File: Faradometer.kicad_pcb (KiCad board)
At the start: 2 copper layers, 26 x 22.2 mm, 20 parts, among them J101 Conn_01x02_Pin, J102 Conn_01x03_Pin, U101 TL072CP, U102 TL072CP

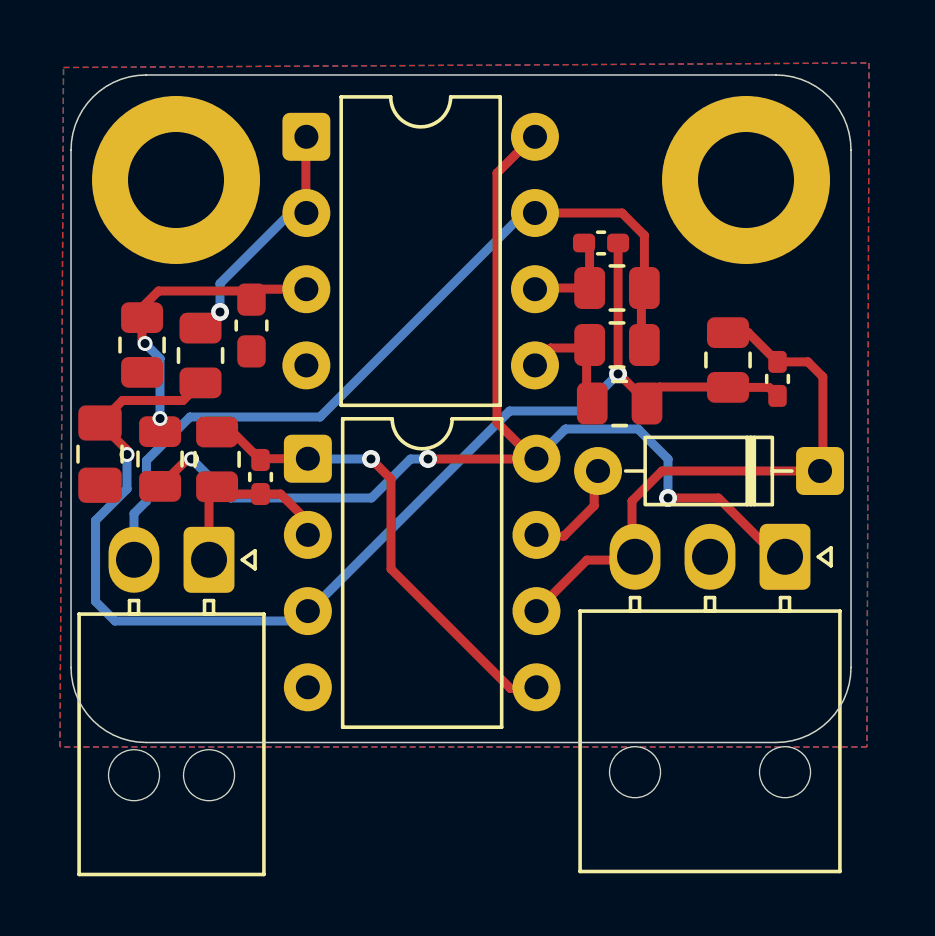
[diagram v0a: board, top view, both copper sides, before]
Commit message: Add .gitignore for KiCad junk files
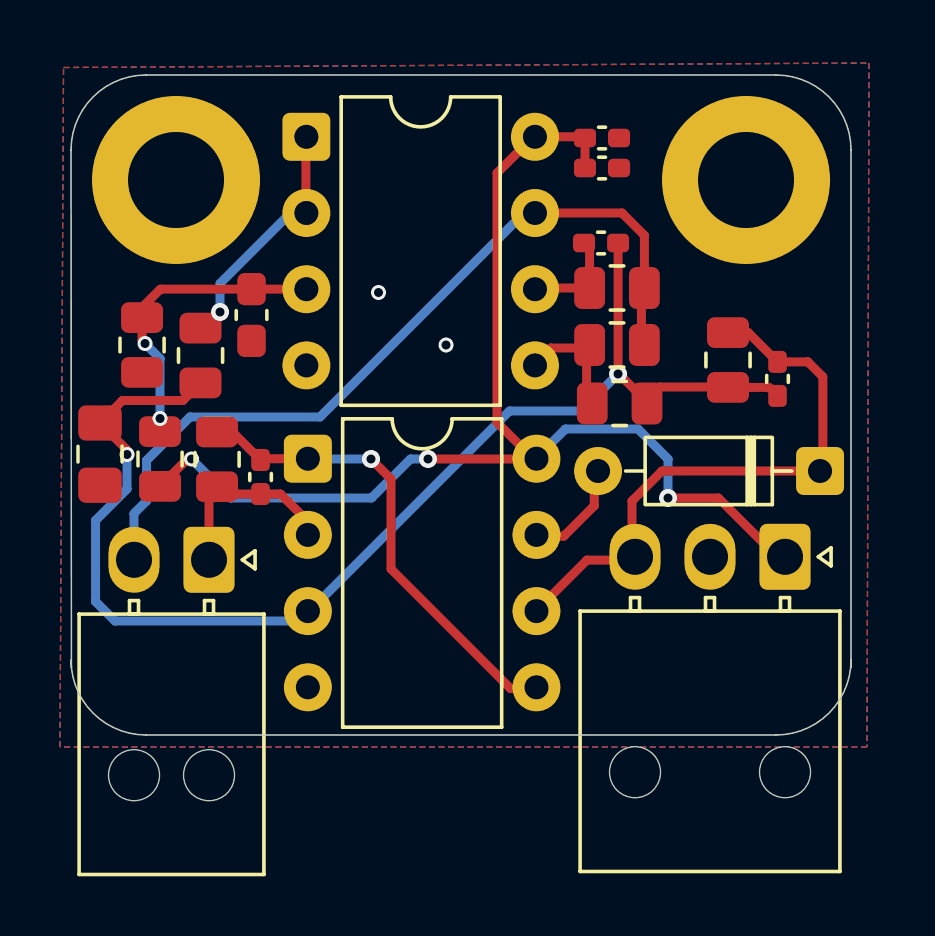
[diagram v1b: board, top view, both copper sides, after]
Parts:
- added C1: 100nF, Capacitor_SMD:C_0402_1005Metric_Pad0.74x0.62mm_HandSolder, F.Cu at (141.7, 65.1)
- added C2: 100nF, Capacitor_SMD:C_0402_1005Metric_Pad0.74x0.62mm_HandSolder, F.Cu at (141.7, 66.1)
- moved C101 0.35 mm to (130.0, 71.0)
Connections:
- net /U2 1 out renamed Net-(U102C-+)
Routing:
- net +12V: track 37.0 -> 39.7 mm
- net GND: vias 0 -> 2
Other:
- board size 26 x 22.2 mm -> 26 x 22 mm

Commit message: decoupling capacitor connection
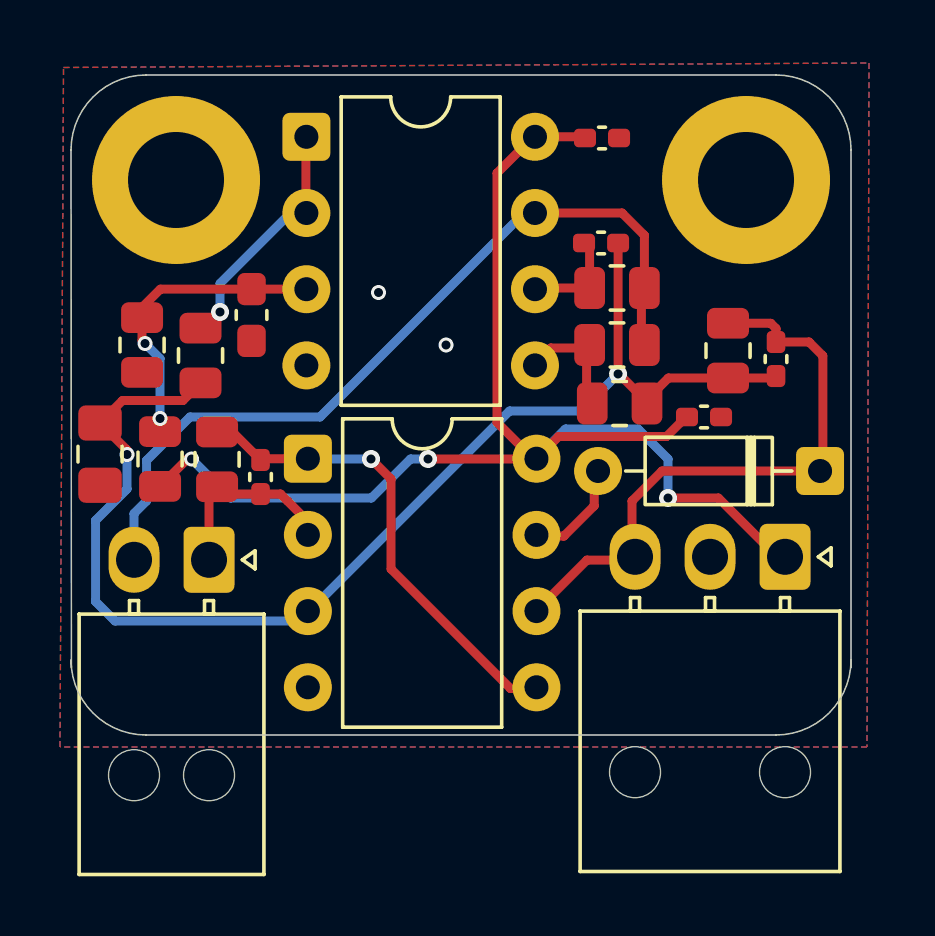
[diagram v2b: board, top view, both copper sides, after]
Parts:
- moved C2 8.97 mm to (145.1, 74.4)
- moved C105 0.66 mm to (147.5, 72.5)
- moved R108 0.31 mm to (145.9, 72.2)
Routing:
- net +12V: track 39.7 -> 44.3 mm
- net /V Out: track 19.6 -> 20.4 mm
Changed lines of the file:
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@@
 	(footprint "Capacitor_SMD:C_0402_1005Metric_Pad0.74x0.62mm_HandSolder"
 		(layer "F.Cu")
-		(at 147.55 73.13 -90)
+		(at 147.5 72.4675 -90)
 		(descr "Capacitor SMD 0402 (1005 Metric), square (rectangular) end terminal, IPC-7351 nominal with elongated pad for handsoldering. (Body size source: IPC-SM-782 page 76, https://www.pcb-3d.com/wordpress/wp-content/uploads/ipc-sm-782a_amendment_1_and_2.pdf), generated with kicad-footprint-generator")
 		(tags "capacitor handsolder")
@@
 	(footprint "Capacitor_SMD:C_0402_1005Metric_Pad0.74x0.62mm_HandSolder"
 		(layer "F.Cu")
-		(at 141.7 66.1)
+		(at 145.1 74.4)
 		(descr "Capacitor SMD 0402 (1005 Metric), square (rectangular) end terminal, IPC-7351 nominal with elongated pad for handsoldering. (Body size source: IPC-SM-782 page 76, https://www.pcb-3d.com/wordpress/wp-content/uploads/ipc-sm-782a_amendment_1_and_2.pdf), generated with kicad-footprint-generator")
 		(tags "capacitor handsolder")
@@
 			(at 0 1.16 0)
 			(layer "F.Fab")
+			(hide yes)
 			(effects
 				(font
@@
 	(footprint "Resistor_SMD:R_0805_2012Metric"
 		(layer "F.Cu")
-		(at 145.9 72.5 90)
+		(at 145.9 72.1875 90)
 		(descr "Resistor SMD 0805 (2012 Metric), square (rectangular) end terminal, IPC-7351 nominal, (Body size source: IPC-SM-782 page 72, https://www.pcb-3d.com/wordpress/wp-content/uploads/ipc-sm-782a_amendment_1_and_2.pdf), generated with kicad-footprint-generator")
 		(tags "resistor")
@@
 	)
 	(segment
-		(start 147.265 73.4125)
-		(end 147.55 73.6975)
+		(start 143.2 73.8125)
+		(end 143.9125 73.1)
 		(width 0.3)
 		(layer "F.Cu")
@@
 	)
 	(segment
-		(start 143.6125 73.4)
-		(end 145.8875 73.4)
+		(start 142.235 72.965)
+		(end 142.235 68.6)
 		(width 0.3)
 		(layer "F.Cu")
@@
 	)
 	(segment
-		(start 142.235 72.965)
-		(end 142.235 68.6)
+		(start 125.8675 75.5)
+		(end 125.8675 75.65)
 		(width 0.3)
 		(layer "F.Cu")
@@
 	)
 	(segment
-		(start 125.8675 75.5)
-		(end 125.8675 75.65)
+		(start 145.9 73.1)
+		(end 147.465 73.1)
 		(width 0.3)
 		(layer "F.Cu")
@@
 	)
 	(segment
-		(start 143.2 73.8125)
-		(end 143.6125 73.4)
-		(width 0.3)
-		(layer "F.Cu")
-		(net 1)
-	)
-	(segment
 		(start 125.7175 73.85)
 		(end 124.9675 74.6)
@@
 	)
 	(segment
-		(start 145.9 73.4125)
-		(end 147.265 73.4125)
+		(start 143.9125 73.1)
+		(end 145.9 73.1)
 		(width 0.3)
 		(layer "F.Cu")
@@
 	)
 	(segment
-		(start 145.8875 73.4)
-		(end 145.9 73.4125)
+		(start 147.465 73.1)
+		(end 147.5 73.135)
+		(width 0.3)
+		(layer "F.Cu")
+		(net 1)
+	)
+	(segment
+		(start 145.8875 73.0875)
+		(end 145.9 73.1)
 		(width 0.3)
 		(layer "F.Cu")
@@
 	)
 	(segment
-		(start 149.06 73.06)
-		(end 148.5625 72.5625)
+		(start 147.325 71.275)
+		(end 145.9 71.275)
 		(width 0.3)
 		(layer "F.Cu")
@@
 	)
 	(segment
-		(start 142.7 77.2)
-		(end 143.7 76.2)
+		(start 147.5 71.9)
+		(end 148.6 71.9)
 		(width 0.3)
 		(layer "F.Cu")
@@
 	)
 	(segment
-		(start 141.1975 79.17)
-		(end 142.65 79.17)
+		(start 139.4575 80.91)
+		(end 139.45 80.91)
 		(width 0.3)
 		(layer "F.Cu")
@@
 	)
 	(segment
-		(start 139.45 80.91)
+		(start 141.1975 79.17)
 		(end 139.4575 80.91)
 		(width 0.3)
@@
 	)
 	(segment
-		(start 148.5625 72.5625)
-		(end 147.55 72.5625)
+		(start 142.65 79.17)
+		(end 141.1975 79.17)
 		(width 0.3)
 		(layer "F.Cu")
@@
 	)
 	(segment
-		(start 142.65 79.17)
-		(end 142.7 79.12)
+		(start 147.5 71.45)
+		(end 147.325 71.275)
 		(width 0.3)
 		(layer "F.Cu")
@@
 	)
 	(segment
-		(start 139.4575 80.91)
-		(end 141.1975 79.17)
+		(start 143.7 76.2)
+		(end 142.7 77.2)
 		(width 0.3)
 		(layer "F.Cu")
@@
 	)
 	(segment
-		(start 142.7 79.12)
-		(end 142.7 77.2)
+		(start 147.5 71.9)
+		(end 147.5 71.45)
 		(width 0.3)
 		(layer "F.Cu")
@@
 	)
 	(segment
-		(start 143.7 76.2)
+		(start 149.06 72.36)
 		(end 149.06 76.2)
 		(width 0.3)
@@
 	)
 	(segment
-		(start 149.06 76.2)
-		(end 149.06 73.06)
+		(start 148.6 71.9)
+		(end 149.06 72.36)
+		(width 0.3)
+		(layer "F.Cu")
+		(net 5)
+	)
+	(segment
+		(start 142.7 79.12)
+		(end 142.65 79.17)
 		(width 0.3)
 		(layer "F.Cu")
@@
 	)
 	(segment
-		(start 145.9 71.5875)
-		(end 146.575 71.5875)
+		(start 142.7 77.2)
+		(end 142.7 79.12)
 		(width 0.3)
 		(layer "F.Cu")
@@
 	)
 	(segment
-		(start 146.575 71.5875)
-		(end 147.55 72.5625)
+		(start 149.06 76.2)
+		(end 143.7 76.2)
 		(width 0.3)
 		(layer "F.Cu")
@@
 	)
 	(segment
-		(start 141.1325 66.1)
-		(end 141.1325 65.1)
+		(start 140.255 75.05)
+		(end 139.515 75.79)
+		(width 0.3)
+		(layer "F.Cu")
+		(net 9)
+	)
+	(segment
+		(start 143.85 75.05)
+		(end 140.255 75.05)
 		(width 0.3)
 		(layer "F.Cu")
@@
 	)
 	(segment
+		(start 144.5325 74.4)
+		(end 144.5 74.4)
+		(width 0.3)
+		(layer "F.Cu")
+		(net 9)
+	)
+	(segment
 		(start 138.2 74.58)
 		(end 139.45 75.83)
@@
 		(width 0.3)
 		(layer "F.Cu")
+		(net 9)
+	)
+	(segment
+		(start 144.5 74.4)
+		(end 143.85 75.05)
+		(width 0.3)
+		(layer "F.Cu")

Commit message: capacitor rearrangements
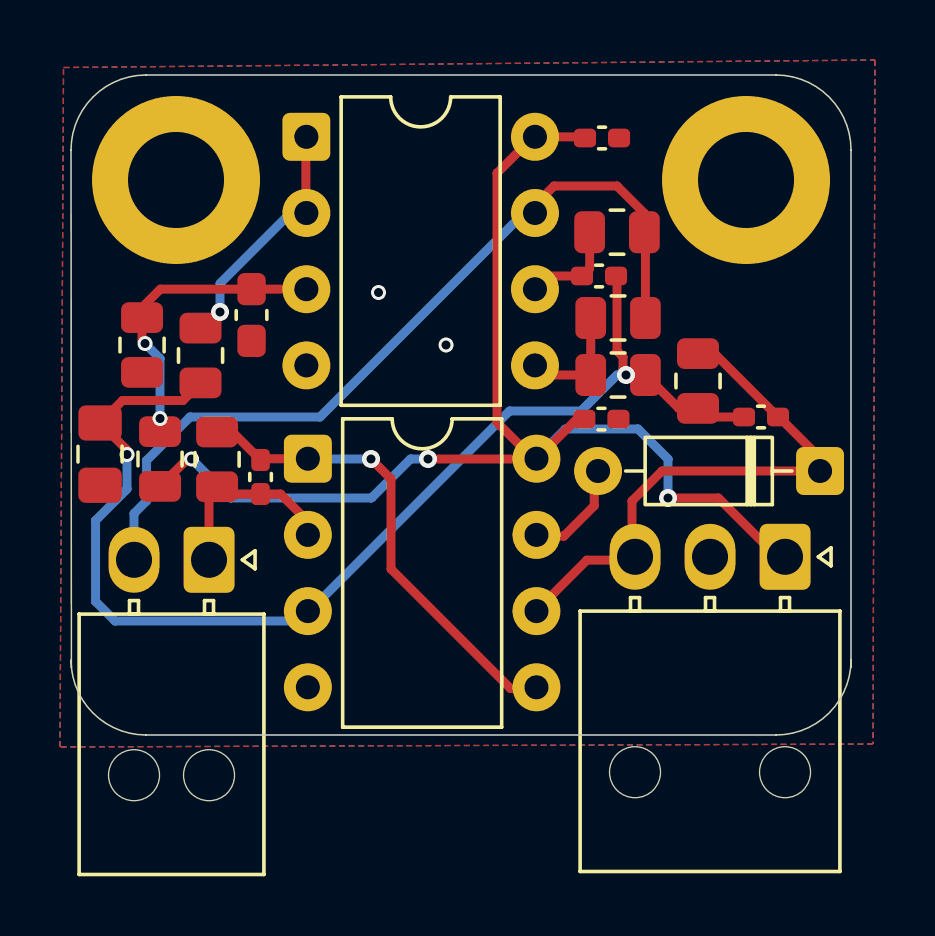
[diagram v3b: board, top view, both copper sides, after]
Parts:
- moved C2 3.42 mm to (141.7, 74.5)
- moved C105 2.00 mm to (147.0, 74.4), turned to 180 degrees
- moved R107 1.86 mm to (142.2, 68.2)
- moved R108 1.42 mm to (144.9, 73.2)
- moved C104 1.10 mm to (141.6, 69.7)
- moved R105 0.95 mm to (142.2, 73.0)
- moved R106 0.90 mm to (142.2, 71.1)
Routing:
- net +12V: track 44.3 -> 40.9 mm
- net /VREF: track 42.2 -> 40.0 mm
- net /V Out: track 20.4 -> 18.6 mm

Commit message: capacitor rearrangements
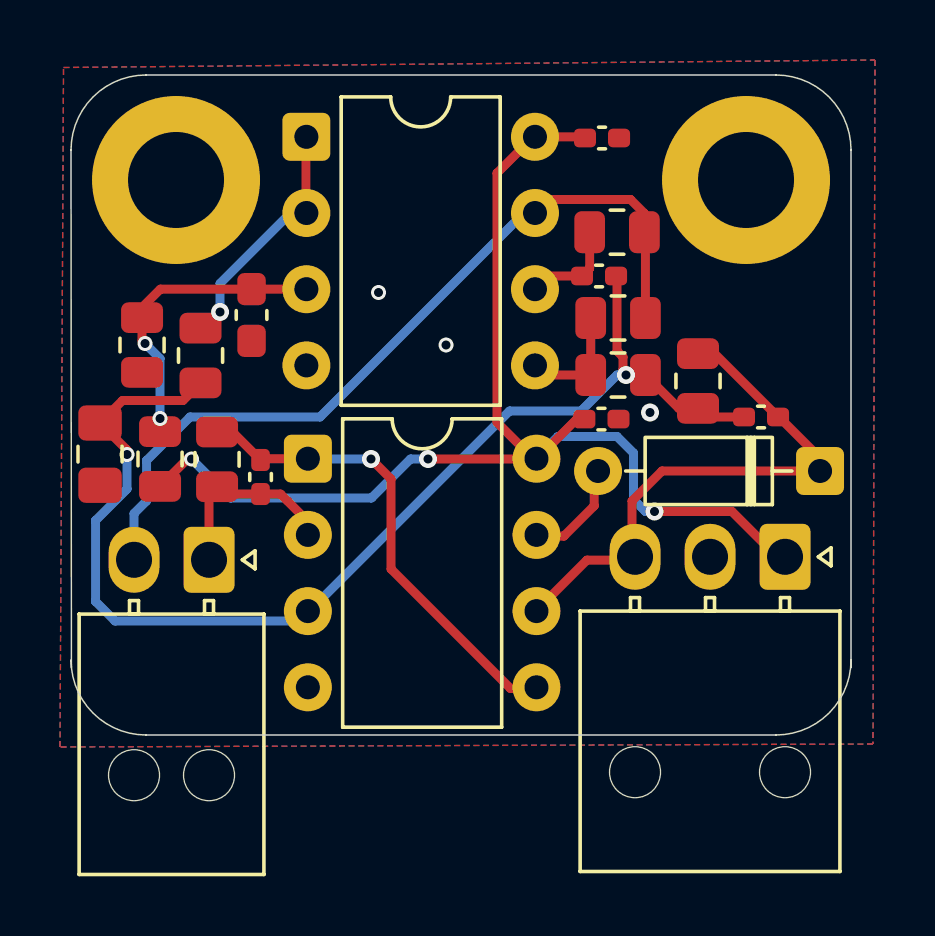
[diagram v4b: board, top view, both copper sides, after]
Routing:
- net GND: vias 2 -> 3
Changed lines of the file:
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@@
 		(net 7)
 	)
-	(segment
-		(start 143.1125 67.6125)
-		(end 143.1125 68.24)
+	(via
+		(at 143.3 74.25)
+		(size 0.6)
+		(drill 0.3)
+		(layers "F.Cu" "B.Cu")
+		(free yes)
+		(net 7)
+	)
+	(segment
+		(start 143.1125 68.24)
+		(end 143.1125 67.6125)
+		(width 0.3)
+		(layer "F.Cu")
+		(net 8)
+	)
+	(segment
+		(start 142.65 67.15)
+		(end 139.65 67.15)
+		(width 0.3)
+		(layer "F.Cu")
+		(net 8)
+	)
+	(segment
+		(start 139.65 67.15)
+		(end 139.465 67.335)
+		(width 0.3)
+		(layer "F.Cu")
+		(net 8)
+	)
+	(segment
+		(start 143.1475 68.27)
+		(end 143.1775 68.24)
+		(width 0.3)
+		(layer "F.Cu")
+		(net 8)
+	)
+	(segment
+		(start 143.1475 71.1)
+		(end 143.1475 68.27)
 		(width 0.3)
 		(layer "F.Cu")
@@
 	)
 	(segment
-		(start 142.2 66.7)
-		(end 143.1125 67.6125)
-		(width 0.3)
-		(layer "F.Cu")
-		(net 8)
-	)
-	(segment
-		(start 143.1475 68.27)
-		(end 143.1775 68.24)
-		(width 0.3)
-		(layer "F.Cu")
-		(net 8)
-	)
-	(segment
-		(start 142.2 66.7)
-		(end 140.1 66.7)
-		(width 0.3)
-		(layer "F.Cu")
-		(net 8)
-	)
-	(segment
-		(start 140.1 66.7)
-		(end 139.465 67.335)
-		(width 0.3)
-		(layer "F.Cu")
-		(net 8)
-	)
-	(segment
-		(start 143.1475 71.1)
-		(end 143.1475 68.27)
+		(start 143.1125 67.6125)
+		(end 142.65 67.15)
 		(width 0.3)
 		(layer "F.Cu")
@@
 	)
 	(segment
+		(start 146.03 77.55)
+		(end 143.45 77.55)
+		(width 0.3)
+		(layer "F.Cu")
+		(net 9)
+	)
+	(segment
 		(start 138.2 74.58)
 		(end 139.45 75.83)
@@
 	)
 	(segment
+		(start 147.65 79.17)
+		(end 146.03 77.55)
+		(width 0.3)
+		(layer "F.Cu")
+		(net 9)
+	)
+	(segment
 		(start 138.2 66.27)
 		(end 138.2 74.58)
@@
 	)
 	(segment
-		(start 145.58 77.1)
-		(end 143.9 77.1)
-		(width 0.3)
-		(layer "F.Cu")
-		(net 9)
-	)
-	(segment
 		(start 141.1325 65.1)
 		(end 141.0925 65.06)
@@
 	)
 	(segment
-		(start 147.65 79.17)
-		(end 145.58 77.1)
-		(width 0.3)
-		(layer "F.Cu")
-		(net 9)
-	)
-	(segment
 		(start 140.8575 74.47)
 		(end 139.5375 75.79)
@@
 	)
 	(via
-		(at 143.9 77.1)
+		(at 143.45 77.55)
 		(size 0.6)
 		(drill 0.3)
@@
 	)
 	(segment
-		(start 140.48 74.8)
-		(end 139.45 75.83)
+		(start 143.15 77.55)
+		(end 142.75 77.15)
 		(width 0.3)
 		(layer "B.Cu")
@@
 	)
 	(segment
-		(start 143.9 75.8)
-		(end 142.9 74.8)
-		(width 0.3)
-		(layer "B.Cu")
-		(net 9)
-	)
-	(segment
-		(start 142.9 74.8)
-		(end 140.48 74.8)
+		(start 140.23 75.05)
+		(end 139.45 75.83)
 		(width 0.3)
 		(layer "B.Cu")
@@
 	)
 	(segment
-		(start 143.9 77.1)
-		(end 143.9 75.8)
+		(start 142.75 75.6)
+		(end 142.2 75.05)
+		(width 0.3)
+		(layer "B.Cu")
+		(net 9)
+	)
+	(segment
+		(start 142.2 75.05)
+		(end 140.23 75.05)
+		(width 0.3)
+		(layer "B.Cu")
+		(net 9)
+	)
+	(segment
+		(start 142.75 77.15)
+		(end 142.75 75.6)
 		(width 0.3)
 		(layer "B.Cu")
@@
 		(width 0.3)
 		(layer "B.Cu")
+		(net 9)
+	)
+	(segment
+		(start 143.45 77.55)
+		(end 143.15 77.55)
+		(width 0.3)
+		(layer "B.Cu")
